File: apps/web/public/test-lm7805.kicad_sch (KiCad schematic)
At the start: 5 parts, among them J1 VIN_CONN, J2 VOUT_5V, U1 LM7805

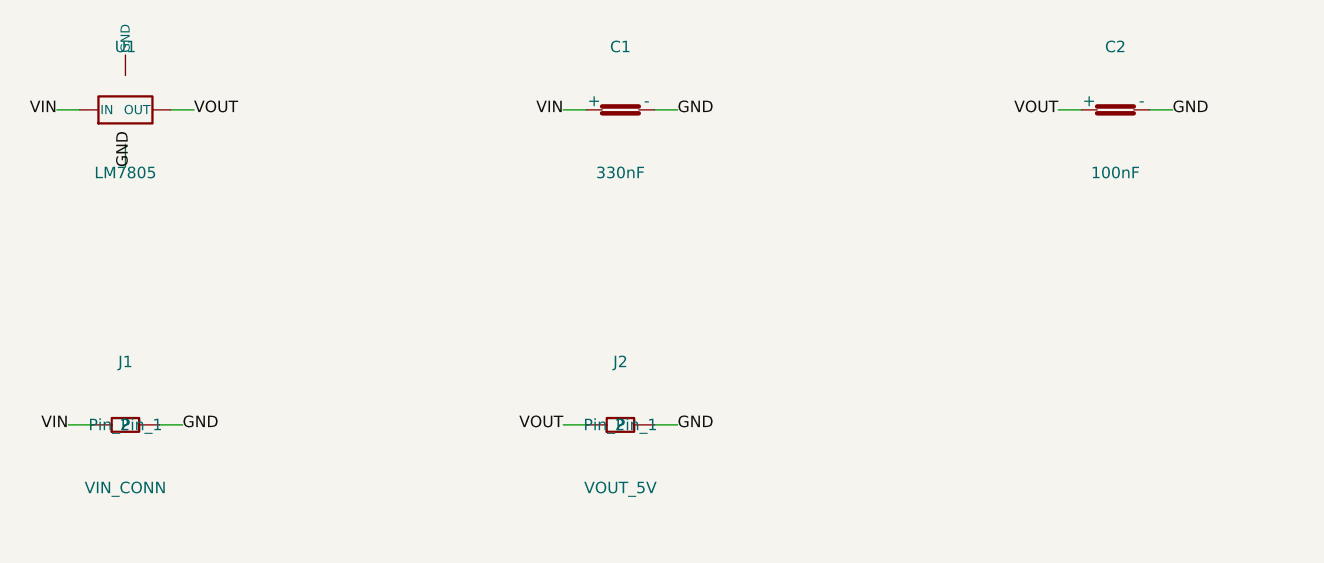
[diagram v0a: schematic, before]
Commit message: fix(schematic): bump margin_side to 38mm + comp_w_span to 20mm for long net-labels
Previous 28mm margin was OK for short labels (VIN, GND) but insufficient
for longer labels like VCC_3V3, LED_GREEN, GND_R2 (~18mm from body centre).
On the ESP32 test schematic, labels GND/VCC_3V3/EN of U1 still touched
the inner frame border.

New values:
- margin_side  = 38mm (was 28) — body origin 38, label text reaches x=20,
  inner frame at x=10 -> 10mm clearance for longest labels
- comp_w_span  = 20mm (was 15) — symmetric clearance on the right side

Paper width grows 181 -> 206mm. All 3 test schematics regenerated.
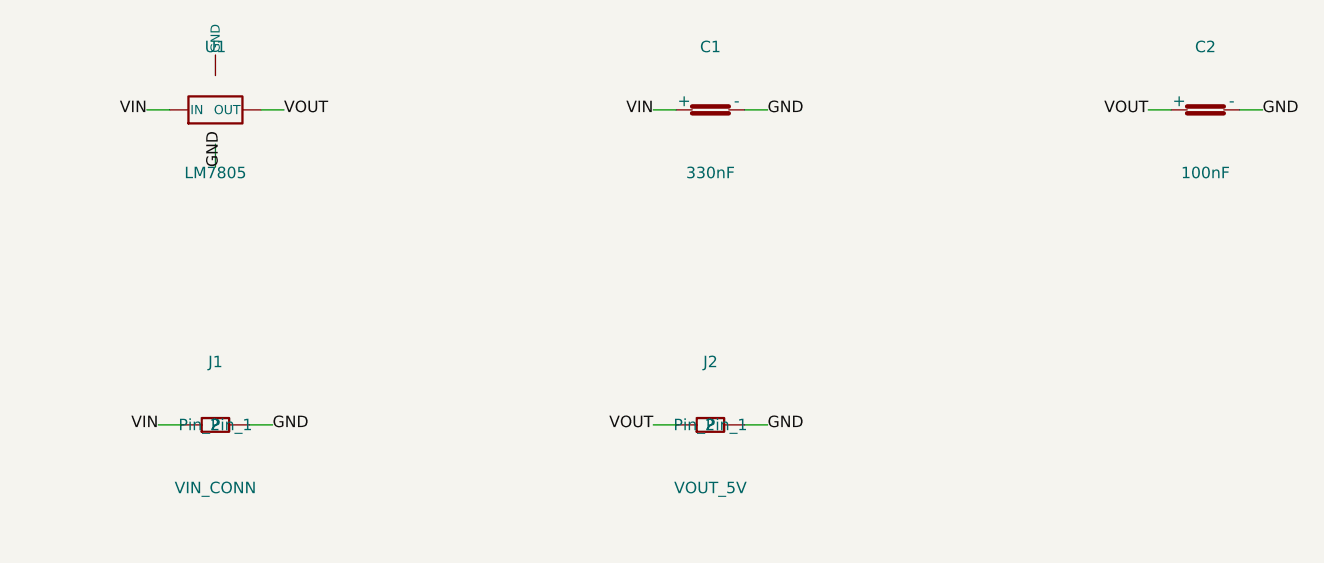
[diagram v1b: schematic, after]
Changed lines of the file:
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@@
 (kicad_sch (version 20230121) (generator "layrix-circuit-synth")
-  (paper "User" 181 123)
-  (symbol (lib_id "Device:VReg_3Pin") (at 28 20 0) (unit 1) (in_bom yes) (on_board yes)
-    (property "Reference" "U1" (at 28 13 0) (effects (font (size 1.27 1.27)) (justify center)))
-    (property "Value" "LM7805" (at 28 27 0) (effects (font (size 1.27 1.27)) (justify center)))
-    (property "Footprint" "Package_TO_SOT_THT:TO-220-3_Vertical" (at 28 30 0) (effects (font (size 1.27 1.27)) (hide yes)))
+  (paper "User" 206 123)
+  (symbol (lib_id "Device:VReg_3Pin") (at 38 20 0) (unit 1) (in_bom yes) (on_board yes)
+    (property "Reference" "U1" (at 38 13 0) (effects (font (size 1.27 1.27)) (justify center)))
+    (property "Value" "LM7805" (at 38 27 0) (effects (font (size 1.27 1.27)) (justify center)))
+    (property "Footprint" "Package_TO_SOT_THT:TO-220-3_Vertical" (at 38 30 0) (effects (font (size 1.27 1.27)) (hide yes)))
   )
-  (symbol (lib_id "Device:C") (at 83 20 0) (unit 1) (in_bom yes) (on_board yes)
-    (property "Reference" "C1" (at 83 13 0) (effects (font (size 1.27 1.27)) (justify center)))
-    (property "Value" "330nF" (at 83 27 0) (effects (font (size 1.27 1.27)) (justify center)))
-    (property "Footprint" "Capacitor_THT:C_Disc_D5.0mm_W2.5mm_P5.00mm" (at 83 30 0) (effects (font (size 1.27 1.27)) (hide yes)))
+  (symbol (lib_id "Device:C") (at 93 20 0) (unit 1) (in_bom yes) (on_board yes)
+    (property "Reference" "C1" (at 93 13 0) (effects (font (size 1.27 1.27)) (justify center)))
+    (property "Value" "330nF" (at 93 27 0) (effects (font (size 1.27 1.27)) (justify center)))
+    (property "Footprint" "Capacitor_THT:C_Disc_D5.0mm_W2.5mm_P5.00mm" (at 93 30 0) (effects (font (size 1.27 1.27)) (hide yes)))
   )
-  (symbol (lib_id "Device:C") (at 138 20 0) (unit 1) (in_bom yes) (on_board yes)
-    (property "Reference" "C2" (at 138 13 0) (effects (font (size 1.27 1.27)) (justify center)))
-    (property "Value" "100nF" (at 138 27 0) (effects (font (size 1.27 1.27)) (justify center)))
-    (property "Footprint" "Capacitor_THT:C_Disc_D5.0mm_W2.5mm_P5.00mm" (at 138 30 0) (effects (font (size 1.27 1.27)) (hide yes)))
+  (symbol (lib_id "Device:C") (at 148 20 0) (unit 1) (in_bom yes) (on_board yes)
+    (property "Reference" "C2" (at 148 13 0) (effects (font (size 1.27 1.27)) (justify center)))
+    (property "Value" "100nF" (at 148 27 0) (effects (font (size 1.27 1.27)) (justify center)))
+    (property "Footprint" "Capacitor_THT:C_Disc_D5.0mm_W2.5mm_P5.00mm" (at 148 30 0) (effects (font (size 1.27 1.27)) (hide yes)))
   )
-  (symbol (lib_id "Connector_Generic:Conn_01x02") (at 28 55 0) (unit 1) (in_bom yes) (on_board yes)
-    (property "Reference" "J1" (at 28 48 0) (effects (font (size 1.27 1.27)) (justify center)))
-    (property "Value" "VIN_CONN" (at 28 62 0) (effects (font (size 1.27 1.27)) (justify center)))
-    (property "Footprint" "Connector_PinHeader_2.54mm:PinHeader_1x02_P2.54mm_Vertical" (at 28 65 0) (effects (font (size 1.27 1.27)) (hide yes)))
+  (symbol (lib_id "Connector_Generic:Conn_01x02") (at 38 55 0) (unit 1) (in_bom yes) (on_board yes)
+    (property "Reference" "J1" (at 38 48 0) (effects (font (size 1.27 1.27)) (justify center)))
+    (property "Value" "VIN_CONN" (at 38 62 0) (effects (font (size 1.27 1.27)) (justify center)))
+    (property "Footprint" "Connector_PinHeader_2.54mm:PinHeader_1x02_P2.54mm_Vertical" (at 38 65 0) (effects (font (size 1.27 1.27)) (hide yes)))
   )
-  (symbol (lib_id "Connector_Generic:Conn_01x02") (at 83 55 0) (unit 1) (in_bom yes) (on_board yes)
-    (property "Reference" "J2" (at 83 48 0) (effects (font (size 1.27 1.27)) (justify center)))
-    (property "Value" "VOUT_5V" (at 83 62 0) (effects (font (size 1.27 1.27)) (justify center)))
-    (property "Footprint" "Connector_PinHeader_2.54mm:PinHeader_1x02_P2.54mm_Vertical" (at 83 65 0) (effects (font (size 1.27 1.27)) (hide yes)))
+  (symbol (lib_id "Connector_Generic:Conn_01x02") (at 93 55 0) (unit 1) (in_bom yes) (on_board yes)
+    (property "Reference" "J2" (at 93 48 0) (effects (font (size 1.27 1.27)) (justify center)))
+    (property "Value" "VOUT_5V" (at 93 62 0) (effects (font (size 1.27 1.27)) (justify center)))
+    (property "Footprint" "Connector_PinHeader_2.54mm:PinHeader_1x02_P2.54mm_Vertical" (at 93 65 0) (effects (font (size 1.27 1.27)) (hide yes)))
   )
-  (wire (pts (xy 22.92 20.0) (xy 20.38 20.0)) (stroke (width 0.1524) (type default)))
-  (label "VIN" (at 20.38 20.0 180) (effects (font (size 1.27 1.27))))
-  (wire (pts (xy 79.19 20.0) (xy 76.65 20.0)) (stroke (width 0.1524) (type default)))
-  (label "VIN" (at 76.65 20.0 180) (effects (font (size 1.27 1.27))))
-  (wire (pts (xy 24.19 55.0) (xy 21.65 55.0)) (stroke (width 0.1524) (type default)))
-  (label "VIN" (at 21.65 55.0 180) (effects (font (size 1.27 1.27))))
-  (wire (pts (xy 28.0 23.81) (xy 28.0 26.35)) (stroke (width 0.1524) (type default)))
-  (label "GND" (at 28.0 26.35 90) (effects (font (size 1.27 1.27))))
-  (wire (pts (xy 86.81 20.0) (xy 89.35 20.0)) (stroke (width 0.1524) (type default)))
-  (label "GND" (at 89.35 20.0 0) (effects (font (size 1.27 1.27))))
-  (wire (pts (xy 141.81 20.0) (xy 144.35 20.0)) (stroke (width 0.1524) (type default)))
-  (label "GND" (at 144.35 20.0 0) (effects (font (size 1.27 1.27))))
-  (wire (pts (xy 31.81 55.0) (xy 34.35 55.0)) (stroke (width 0.1524) (type default)))
-  (label "GND" (at 34.35 55.0 0) (effects (font (size 1.27 1.27))))
-  (wire (pts (xy 86.81 55.0) (xy 89.35 55.0)) (stroke (width 0.1524) (type default)))
-  (label "GND" (at 89.35 55.0 0) (effects (font (size 1.27 1.27))))
-  (wire (pts (xy 33.08 20.0) (xy 35.62 20.0)) (stroke (width 0.1524) (type default)))
-  (label "VOUT" (at 35.62 20.0 0) (effects (font (size 1.27 1.27))))
-  (wire (pts (xy 134.19 20.0) (xy 131.65 20.0)) (stroke (width 0.1524) (type default)))
-  (label "VOUT" (at 131.65 20.0 180) (effects (font (size 1.27 1.27))))
-  (wire (pts (xy 79.19 55.0) (xy 76.65 55.0)) (stroke (width 0.1524) (type default)))
-  (label "VOUT" (at 76.65 55.0 180) (effects (font (size 1.27 1.27))))
+  (wire (pts (xy 32.92 20.0) (xy 30.38 20.0)) (stroke (width 0.1524) (type default)))
+  (label "VIN" (at 30.38 20.0 180) (effects (font (size 1.27 1.27))))
+  (wire (pts (xy 89.19 20.0) (xy 86.65 20.0)) (stroke (width 0.1524) (type default)))
+  (label "VIN" (at 86.65 20.0 180) (effects (font (size 1.27 1.27))))
+  (wire (pts (xy 34.19 55.0) (xy 31.65 55.0)) (stroke (width 0.1524) (type default)))
+  (label "VIN" (at 31.65 55.0 180) (effects (font (size 1.27 1.27))))
+  (wire (pts (xy 38.0 23.81) (xy 38.0 26.35)) (stroke (width 0.1524) (type default)))
+  (label "GND" (at 38.0 26.35 90) (effects (font (size 1.27 1.27))))
+  (wire (pts (xy 96.81 20.0) (xy 99.35 20.0)) (stroke (width 0.1524) (type default)))
+  (label "GND" (at 99.35 20.0 0) (effects (font (size 1.27 1.27))))
+  (wire (pts (xy 151.81 20.0) (xy 154.35 20.0)) (stroke (width 0.1524) (type default)))
+  (label "GND" (at 154.35 20.0 0) (effects (font (size 1.27 1.27))))
+  (wire (pts (xy 41.81 55.0) (xy 44.35 55.0)) (stroke (width 0.1524) (type default)))
+  (label "GND" (at 44.35 55.0 0) (effects (font (size 1.27 1.27))))
+  (wire (pts (xy 96.81 55.0) (xy 99.35 55.0)) (stroke (width 0.1524) (type default)))
+  (label "GND" (at 99.35 55.0 0) (effects (font (size 1.27 1.27))))
+  (wire (pts (xy 43.08 20.0) (xy 45.62 20.0)) (stroke (width 0.1524) (type default)))
+  (label "VOUT" (at 45.62 20.0 0) (effects (font (size 1.27 1.27))))
+  (wire (pts (xy 144.19 20.0) (xy 141.65 20.0)) (stroke (width 0.1524) (type default)))
+  (label "VOUT" (at 141.65 20.0 180) (effects (font (size 1.27 1.27))))
+  (wire (pts (xy 89.19 55.0) (xy 86.65 55.0)) (stroke (width 0.1524) (type default)))
+  (label "VOUT" (at 86.65 55.0 180) (effects (font (size 1.27 1.27))))
   (sheet_instances (path "/" (page "1")))
 )

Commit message: fix(schematic): more breathing room — bump margin_top to 25mm + TITLE_PADDING to 15mm
Component names (Reference U1/C1/J1 + Value LM7805/330nF/VIN_CONN) were
visually too close to the inner frame top border and to the title block
edge. Increased internal margins so all labels sit comfortably inside
the visible inner frame area.

Changes:
- margin_top      20 -> 25 mm  (more space below the upper frame border)
- TITLE_PADDING    6 -> 15 mm  (more space before the title block)
- Paper height grows 123 -> 137 mm (LM7805) / 158 -> 172 mm (NE555/ESP32)
- Regenerated all 3 test schematics

Verified visually: U1+LM7805, C1+330nF, C2+100nF, J1+VIN_CONN,
J2+VOUT_5V all sit inside the inner frame with clear buffer on all sides.
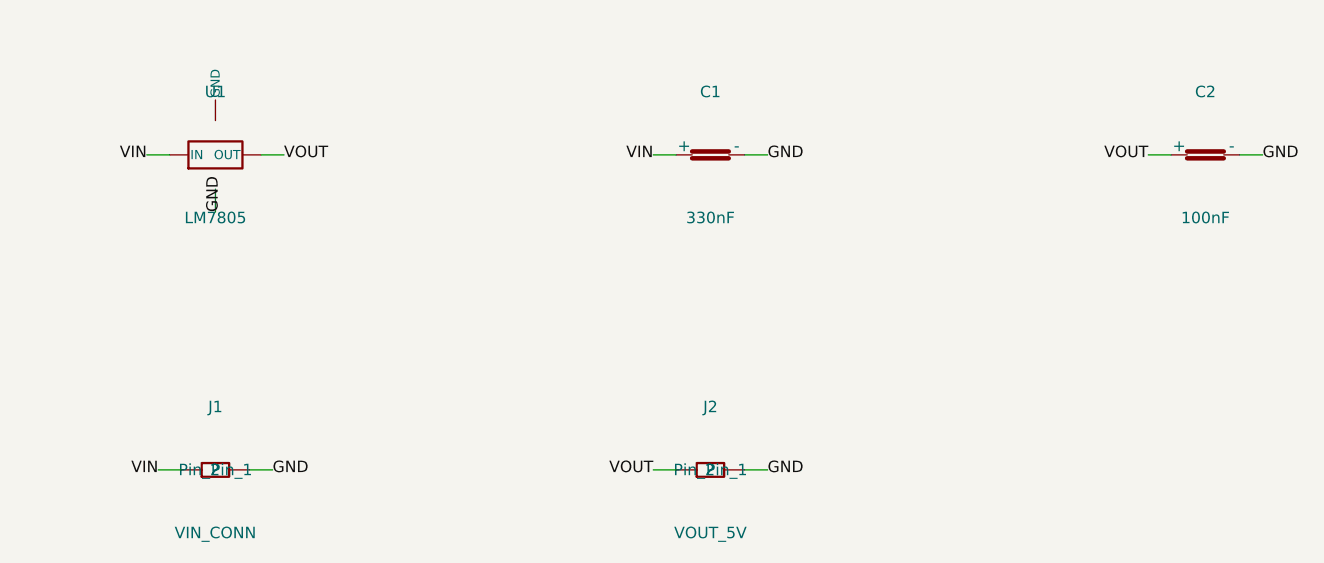
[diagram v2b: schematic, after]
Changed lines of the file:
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@@
 (kicad_sch (version 20230121) (generator "layrix-circuit-synth")
-  (paper "User" 206 123)
-  (symbol (lib_id "Device:VReg_3Pin") (at 38 20 0) (unit 1) (in_bom yes) (on_board yes)
-    (property "Reference" "U1" (at 38 13 0) (effects (font (size 1.27 1.27)) (justify center)))
-    (property "Value" "LM7805" (at 38 27 0) (effects (font (size 1.27 1.27)) (justify center)))
-    (property "Footprint" "Package_TO_SOT_THT:TO-220-3_Vertical" (at 38 30 0) (effects (font (size 1.27 1.27)) (hide yes)))
+  (paper "User" 206 137)
+  (symbol (lib_id "Device:VReg_3Pin") (at 38 25 0) (unit 1) (in_bom yes) (on_board yes)
+    (property "Reference" "U1" (at 38 18 0) (effects (font (size 1.27 1.27)) (justify center)))
+    (property "Value" "LM7805" (at 38 32 0) (effects (font (size 1.27 1.27)) (justify center)))
+    (property "Footprint" "Package_TO_SOT_THT:TO-220-3_Vertical" (at 38 35 0) (effects (font (size 1.27 1.27)) (hide yes)))
   )
-  (symbol (lib_id "Device:C") (at 93 20 0) (unit 1) (in_bom yes) (on_board yes)
-    (property "Reference" "C1" (at 93 13 0) (effects (font (size 1.27 1.27)) (justify center)))
-    (property "Value" "330nF" (at 93 27 0) (effects (font (size 1.27 1.27)) (justify center)))
-    (property "Footprint" "Capacitor_THT:C_Disc_D5.0mm_W2.5mm_P5.00mm" (at 93 30 0) (effects (font (size 1.27 1.27)) (hide yes)))
+  (symbol (lib_id "Device:C") (at 93 25 0) (unit 1) (in_bom yes) (on_board yes)
+    (property "Reference" "C1" (at 93 18 0) (effects (font (size 1.27 1.27)) (justify center)))
+    (property "Value" "330nF" (at 93 32 0) (effects (font (size 1.27 1.27)) (justify center)))
+    (property "Footprint" "Capacitor_THT:C_Disc_D5.0mm_W2.5mm_P5.00mm" (at 93 35 0) (effects (font (size 1.27 1.27)) (hide yes)))
   )
-  (symbol (lib_id "Device:C") (at 148 20 0) (unit 1) (in_bom yes) (on_board yes)
-    (property "Reference" "C2" (at 148 13 0) (effects (font (size 1.27 1.27)) (justify center)))
-    (property "Value" "100nF" (at 148 27 0) (effects (font (size 1.27 1.27)) (justify center)))
-    (property "Footprint" "Capacitor_THT:C_Disc_D5.0mm_W2.5mm_P5.00mm" (at 148 30 0) (effects (font (size 1.27 1.27)) (hide yes)))
+  (symbol (lib_id "Device:C") (at 148 25 0) (unit 1) (in_bom yes) (on_board yes)
+    (property "Reference" "C2" (at 148 18 0) (effects (font (size 1.27 1.27)) (justify center)))
+    (property "Value" "100nF" (at 148 32 0) (effects (font (size 1.27 1.27)) (justify center)))
+    (property "Footprint" "Capacitor_THT:C_Disc_D5.0mm_W2.5mm_P5.00mm" (at 148 35 0) (effects (font (size 1.27 1.27)) (hide yes)))
   )
-  (symbol (lib_id "Connector_Generic:Conn_01x02") (at 38 55 0) (unit 1) (in_bom yes) (on_board yes)
-    (property "Reference" "J1" (at 38 48 0) (effects (font (size 1.27 1.27)) (justify center)))
-    (property "Value" "VIN_CONN" (at 38 62 0) (effects (font (size 1.27 1.27)) (justify center)))
-    (property "Footprint" "Connector_PinHeader_2.54mm:PinHeader_1x02_P2.54mm_Vertical" (at 38 65 0) (effects (font (size 1.27 1.27)) (hide yes)))
+  (symbol (lib_id "Connector_Generic:Conn_01x02") (at 38 60 0) (unit 1) (in_bom yes) (on_board yes)
+    (property "Reference" "J1" (at 38 53 0) (effects (font (size 1.27 1.27)) (justify center)))
+    (property "Value" "VIN_CONN" (at 38 67 0) (effects (font (size 1.27 1.27)) (justify center)))
+    (property "Footprint" "Connector_PinHeader_2.54mm:PinHeader_1x02_P2.54mm_Vertical" (at 38 70 0) (effects (font (size 1.27 1.27)) (hide yes)))
   )
-  (symbol (lib_id "Connector_Generic:Conn_01x02") (at 93 55 0) (unit 1) (in_bom yes) (on_board yes)
-    (property "Reference" "J2" (at 93 48 0) (effects (font (size 1.27 1.27)) (justify center)))
-    (property "Value" "VOUT_5V" (at 93 62 0) (effects (font (size 1.27 1.27)) (justify center)))
-    (property "Footprint" "Connector_PinHeader_2.54mm:PinHeader_1x02_P2.54mm_Vertical" (at 93 65 0) (effects (font (size 1.27 1.27)) (hide yes)))
+  (symbol (lib_id "Connector_Generic:Conn_01x02") (at 93 60 0) (unit 1) (in_bom yes) (on_board yes)
+    (property "Reference" "J2" (at 93 53 0) (effects (font (size 1.27 1.27)) (justify center)))
+    (property "Value" "VOUT_5V" (at 93 67 0) (effects (font (size 1.27 1.27)) (justify center)))
+    (property "Footprint" "Connector_PinHeader_2.54mm:PinHeader_1x02_P2.54mm_Vertical" (at 93 70 0) (effects (font (size 1.27 1.27)) (hide yes)))
   )
-  (wire (pts (xy 32.92 20.0) (xy 30.38 20.0)) (stroke (width 0.1524) (type default)))
-  (label "VIN" (at 30.38 20.0 180) (effects (font (size 1.27 1.27))))
-  (wire (pts (xy 89.19 20.0) (xy 86.65 20.0)) (stroke (width 0.1524) (type default)))
-  (label "VIN" (at 86.65 20.0 180) (effects (font (size 1.27 1.27))))
-  (wire (pts (xy 34.19 55.0) (xy 31.65 55.0)) (stroke (width 0.1524) (type default)))
-  (label "VIN" (at 31.65 55.0 180) (effects (font (size 1.27 1.27))))
-  (wire (pts (xy 38.0 23.81) (xy 38.0 26.35)) (stroke (width 0.1524) (type default)))
-  (label "GND" (at 38.0 26.35 90) (effects (font (size 1.27 1.27))))
-  (wire (pts (xy 96.81 20.0) (xy 99.35 20.0)) (stroke (width 0.1524) (type default)))
-  (label "GND" (at 99.35 20.0 0) (effects (font (size 1.27 1.27))))
-  (wire (pts (xy 151.81 20.0) (xy 154.35 20.0)) (stroke (width 0.1524) (type default)))
-  (label "GND" (at 154.35 20.0 0) (effects (font (size 1.27 1.27))))
-  (wire (pts (xy 41.81 55.0) (xy 44.35 55.0)) (stroke (width 0.1524) (type default)))
-  (label "GND" (at 44.35 55.0 0) (effects (font (size 1.27 1.27))))
-  (wire (pts (xy 96.81 55.0) (xy 99.35 55.0)) (stroke (width 0.1524) (type default)))
-  (label "GND" (at 99.35 55.0 0) (effects (font (size 1.27 1.27))))
-  (wire (pts (xy 43.08 20.0) (xy 45.62 20.0)) (stroke (width 0.1524) (type default)))
-  (label "VOUT" (at 45.62 20.0 0) (effects (font (size 1.27 1.27))))
-  (wire (pts (xy 144.19 20.0) (xy 141.65 20.0)) (stroke (width 0.1524) (type default)))
-  (label "VOUT" (at 141.65 20.0 180) (effects (font (size 1.27 1.27))))
-  (wire (pts (xy 89.19 55.0) (xy 86.65 55.0)) (stroke (width 0.1524) (type default)))
-  (label "VOUT" (at 86.65 55.0 180) (effects (font (size 1.27 1.27))))
+  (wire (pts (xy 32.92 25.0) (xy 30.38 25.0)) (stroke (width 0.1524) (type default)))
+  (label "VIN" (at 30.38 25.0 180) (effects (font (size 1.27 1.27))))
+  (wire (pts (xy 89.19 25.0) (xy 86.65 25.0)) (stroke (width 0.1524) (type default)))
+  (label "VIN" (at 86.65 25.0 180) (effects (font (size 1.27 1.27))))
+  (wire (pts (xy 34.19 60.0) (xy 31.65 60.0)) (stroke (width 0.1524) (type default)))
+  (label "VIN" (at 31.65 60.0 180) (effects (font (size 1.27 1.27))))
+  (wire (pts (xy 38.0 28.81) (xy 38.0 31.35)) (stroke (width 0.1524) (type default)))
+  (label "GND" (at 38.0 31.35 90) (effects (font (size 1.27 1.27))))
+  (wire (pts (xy 96.81 25.0) (xy 99.35 25.0)) (stroke (width 0.1524) (type default)))
+  (label "GND" (at 99.35 25.0 0) (effects (font (size 1.27 1.27))))
+  (wire (pts (xy 151.81 25.0) (xy 154.35 25.0)) (stroke (width 0.1524) (type default)))
+  (label "GND" (at 154.35 25.0 0) (effects (font (size 1.27 1.27))))
+  (wire (pts (xy 41.81 60.0) (xy 44.35 60.0)) (stroke (width 0.1524) (type default)))
+  (label "GND" (at 44.35 60.0 0) (effects (font (size 1.27 1.27))))
+  (wire (pts (xy 96.81 60.0) (xy 99.35 60.0)) (stroke (width 0.1524) (type default)))
+  (label "GND" (at 99.35 60.0 0) (effects (font (size 1.27 1.27))))
+  (wire (pts (xy 43.08 25.0) (xy 45.62 25.0)) (stroke (width 0.1524) (type default)))
+  (label "VOUT" (at 45.62 25.0 0) (effects (font (size 1.27 1.27))))
+  (wire (pts (xy 144.19 25.0) (xy 141.65 25.0)) (stroke (width 0.1524) (type default)))
+  (label "VOUT" (at 141.65 25.0 180) (effects (font (size 1.27 1.27))))
+  (wire (pts (xy 89.19 60.0) (xy 86.65 60.0)) (stroke (width 0.1524) (type default)))
+  (label "VOUT" (at 86.65 60.0 180) (effects (font (size 1.27 1.27))))
   (sheet_instances (path "/" (page "1")))
 )
